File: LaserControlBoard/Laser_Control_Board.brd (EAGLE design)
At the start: 50.8 x 50.8 mm, 36 parts, among them J1 Servo Header, J2 FTDI Header, J5 FEMALE 2x3, J6 455-1750-1-ND, U1 ATMEGA328P_TQFP, Y1 16MHz

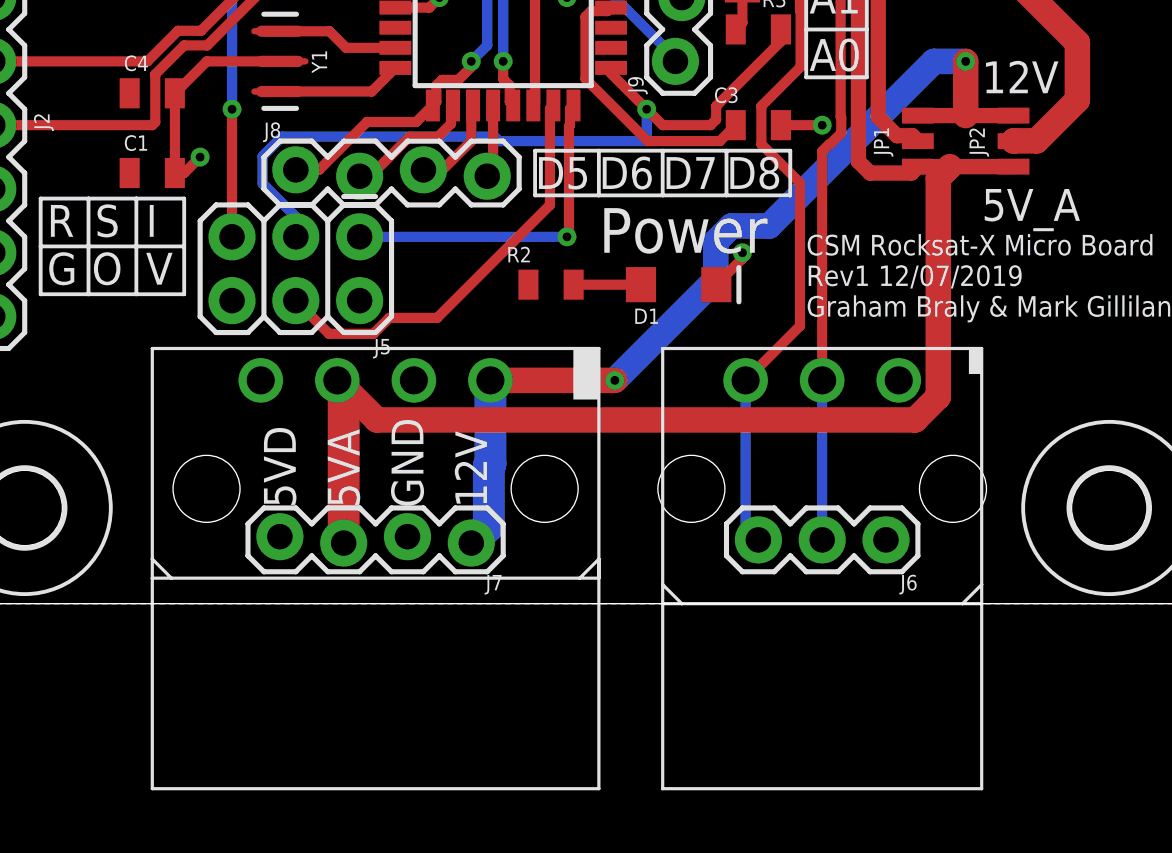
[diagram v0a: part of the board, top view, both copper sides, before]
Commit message: Improved Molex connector footprints.
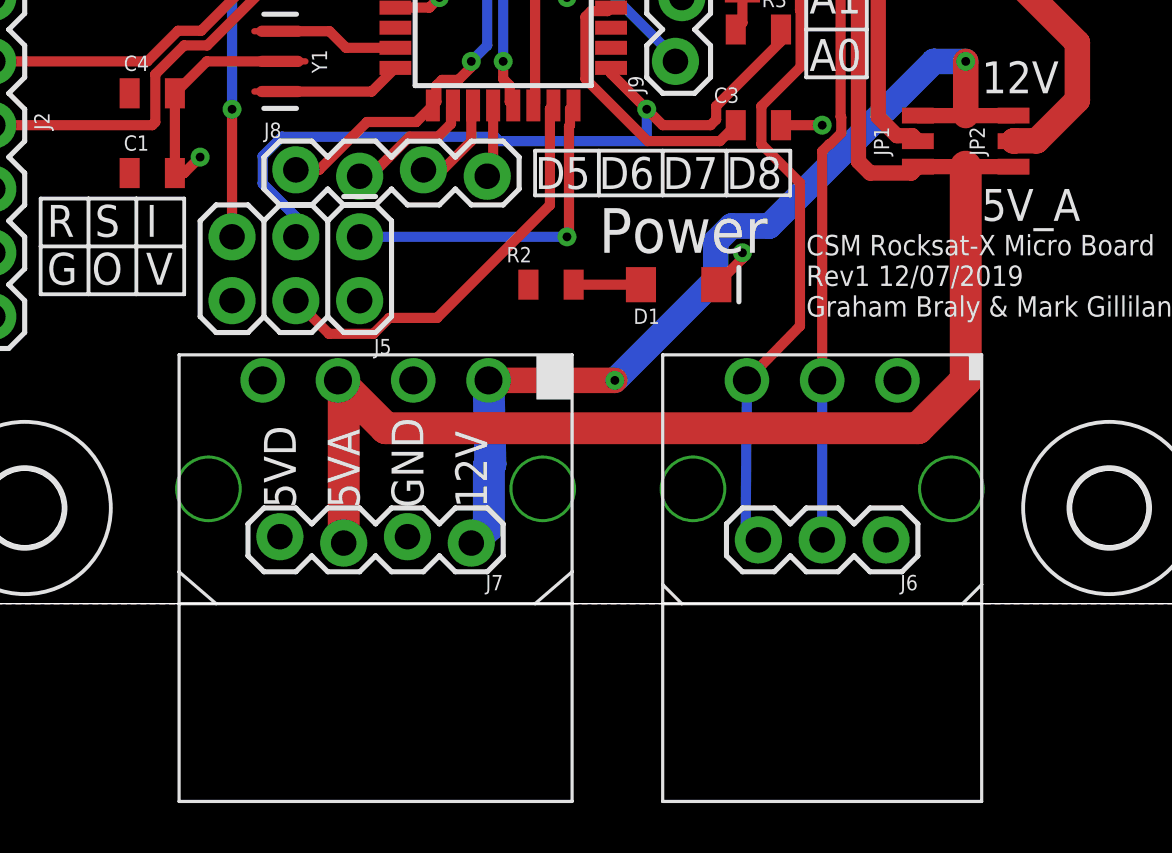
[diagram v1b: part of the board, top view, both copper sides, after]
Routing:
- net 5V_ACT: track 89.7 -> 90.5 mm
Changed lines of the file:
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@@
 <attribute name="VALUE" x="8.89" y="46.228" size="0.6096" layer="27" font="vector" ratio="20"/>
 </element>
-<element name="H1" library="holes" library_urn="urn:adsk.eagle:library:237" package="3,0" package3d_urn="urn:adsk.eagle:package:14277/1" value="MOUNT-HOLE3.0" x="3.81" y="3.81" smashed="yes"/>
-<element name="H2" library="holes" library_urn="urn:adsk.eagle:library:237" package="3,0" package3d_urn="urn:adsk.eagle:package:14277/1" value="MOUNT-HOLE3.0" x="46.99" y="3.81" smashed="yes"/>
-<element name="H3" library="holes" library_urn="urn:adsk.eagle:library:237" package="3,0" package3d_urn="urn:adsk.eagle:package:14277/1" value="MOUNT-HOLE3.0" x="3.81" y="46.99" smashed="yes"/>
-<element name="H4" library="holes" library_urn="urn:adsk.eagle:library:237" package="3,0" package3d_urn="urn:adsk.eagle:package:14277/1" value="MOUNT-HOLE3.0" x="46.99" y="46.99" smashed="yes"/>
+<element name="H1" library="holes" library_urn="urn:adsk.eagle:library:237" package="3,0" package3d_urn="urn:adsk.eagle:package:14277/1" value="MOUNT-HOLE3.0" x="3.81" y="3.81" smashed="yes">
+<attribute name="POPULARITY" value="3" x="3.81" y="3.81" size="1.778" layer="27" display="off"/>
+</element>
+<element name="H2" library="holes" library_urn="urn:adsk.eagle:library:237" package="3,0" package3d_urn="urn:adsk.eagle:package:14277/1" value="MOUNT-HOLE3.0" x="46.99" y="3.81" smashed="yes">
+<attribute name="POPULARITY" value="3" x="46.99" y="3.81" size="1.778" layer="27" display="off"/>
+</element>
+<element name="H3" library="holes" library_urn="urn:adsk.eagle:library:237" package="3,0" package3d_urn="urn:adsk.eagle:package:14277/1" value="MOUNT-HOLE3.0" x="3.81" y="46.99" smashed="yes">
+<attribute name="POPULARITY" value="3" x="3.81" y="46.99" size="1.778" layer="27" display="off"/>
+</element>
+<element name="H4" library="holes" library_urn="urn:adsk.eagle:library:237" package="3,0" package3d_urn="urn:adsk.eagle:package:14277/1" value="MOUNT-HOLE3.0" x="46.99" y="46.99" smashed="yes">
+<attribute name="POPULARITY" value="3" x="46.99" y="46.99" size="1.778" layer="27" display="off"/>
+</element>
 <element name="S1" library="SparkFun-Switches" package="TACTILE_SWITCH_SMD_5.2MM" value="RESET" x="25.4" y="38.1" smashed="yes" rot="R90">
 <attribute name="NAME" x="22.733" y="38.1" size="0.6096" layer="25" font="vector" ratio="20" rot="R90" align="bottom-center"/>
@@
 <element name="D2" library="diode" library_urn="urn:adsk.eagle:library:210" package="SMA" package3d_urn="urn:adsk.eagle:package:43460/3" value="S1M" x="39.37" y="27.94" smashed="yes" rot="R270">
 <attribute name="NAME" x="41.37" y="30.69" size="1.27" layer="25" ratio="10" rot="R270"/>
+<attribute name="POPULARITY" value="0" x="39.37" y="27.94" size="1.778" layer="27" rot="R270" display="off"/>
 <attribute name="VALUE" x="41.585" y="28.15" size="1.27" layer="27" ratio="10" rot="R270"/>
 </element>
@@
 <element name="D4" library="diode" library_urn="urn:adsk.eagle:library:210" package="SMA" package3d_urn="urn:adsk.eagle:package:43460/3" value="S1M" x="45.085" y="27.94" smashed="yes" rot="R270">
 <attribute name="NAME" x="47.085" y="30.69" size="1.27" layer="25" ratio="10" rot="R270"/>
+<attribute name="POPULARITY" value="0" x="45.085" y="27.94" size="1.778" layer="27" rot="R270" display="off"/>
 <attribute name="VALUE" x="47.3" y="28.15" size="1.27" layer="27" ratio="10" rot="R270"/>
 </element>
@@
 <wire x1="39.37" y1="19.431" x2="41.275" y2="19.431" width="0.6096" layer="1"/>
 <wire x1="41.275" y1="19.431" x2="43.18" y2="19.431" width="0.6096" layer="1"/>
-<wire x1="22.352" y1="8.89" x2="27.305" y2="8.89" width="1.016" layer="1"/>
+<wire x1="22.2758" y1="8.89" x2="27.305" y2="8.89" width="1.016" layer="1"/>
 <via x="27.305" y="8.89" extent="1-16" drill="0.35"/>
 <wire x1="40.005" y1="21.59" x2="41.275" y2="21.59" width="1.016" layer="16"/>
@@
 <wire x1="41.275" y1="21.59" x2="41.275" y2="19.431" width="1.016" layer="1"/>
 <contactref element="J7" pad="1"/>
-<wire x1="22.352" y1="8.89" x2="22.352" y2="5.55609375" width="1.27" layer="16"/>
+<wire x1="22.2758" y1="8.89" x2="22.352" y2="5.55609375" width="1.27" layer="16"/>
 <wire x1="22.352" y1="5.55609375" x2="22.2885" y2="5.49259375" width="1.27" layer="16"/>
 <wire x1="22.2885" y1="3.1115" x2="21.59" y2="2.413" width="1.27" layer="16"/>
@@
 <contactref element="JP1" pad="1"/>
 <contactref element="JP2" pad="1"/>
-<wire x1="39.37" y1="17.399" x2="40.64" y2="17.399" width="0.6096" layer="1"/>
-<wire x1="40.64" y1="17.399" x2="43.18" y2="17.399" width="0.6096" layer="1"/>
+<wire x1="39.37" y1="17.399" x2="41.275" y2="17.399" width="0.6096" layer="1"/>
+<wire x1="41.275" y1="17.399" x2="43.18" y2="17.399" width="0.6096" layer="1"/>
 <wire x1="37.005" y1="17.605" x2="37.465" y2="17.145" width="0.6096" layer="1"/>
 <wire x1="37.005" y1="17.605" x2="37.005" y2="27.02105625" width="0.6096" layer="1"/>
 <wire x1="37.465" y1="17.145" x2="39.116" y2="17.145" width="0.6096" layer="1"/>
 <wire x1="39.116" y1="17.145" x2="39.37" y2="17.399" width="0.6096" layer="1"/>
-<wire x1="39.26030625" y1="7.3152" x2="40.1828" y2="8.23769375" width="1.016" layer="1"/>
-<wire x1="40.1828" y1="16.9418" x2="40.64" y2="17.399" width="1.016" layer="1"/>
-<wire x1="40.1828" y1="8.23769375" x2="40.1828" y2="16.9418" width="1.016" layer="1"/>
 <wire x1="28.575" y1="35.45105625" x2="28.575" y2="42.545" width="0.6096" layer="1"/>
 <wire x1="28.575" y1="42.545" x2="26.67" y2="44.45" width="0.6096" layer="1"/>
 <wire x1="26.67" y1="44.45" x2="20.955" y2="44.45" width="0.6096" layer="1"/>
 <wire x1="37.005" y1="27.02105625" x2="28.575" y2="35.45105625" width="0.6096" layer="1"/>
-<wire x1="16.256" y1="8.89" x2="17.8308" y2="7.3152" width="1.016" layer="1"/>
-<wire x1="17.8308" y1="7.3152" x2="39.26030625" y2="7.3152" width="1.016" layer="1"/>
 <contactref element="J7" pad="3"/>
-<wire x1="16.256" y1="8.89" x2="16.51" y2="8.636" width="1.27" layer="1"/>
+<wire x1="16.2814" y1="8.89" x2="16.51" y2="8.636" width="1.27" layer="1"/>
 <wire x1="16.51" y1="8.636" x2="16.51" y2="2.413" width="1.27" layer="1"/>
+<wire x1="16.2814" y1="8.89" x2="18.1864" y2="6.985" width="1.27" layer="1"/>
+<wire x1="39.37" y1="6.985" x2="41.275" y2="8.89" width="1.27" layer="1"/>
+<wire x1="41.275" y1="8.89" x2="41.275" y2="17.399" width="1.27" layer="1"/>
+<wire x1="18.1864" y1="6.985" x2="39.37" y2="6.985" width="1.27" layer="1"/>
 </signal>
 <signal name="SDA">
@@
 <wire x1="24.06" y1="28.4226" x2="24.1996" y2="28.5622" width="0.4064" layer="1"/>
 <wire x1="24.1996" y1="28.5622" x2="24.1996" y2="29.2154125" width="0.4064" layer="1"/>
-<wire x1="34.6756" y1="11.0536" x2="32.512" y2="8.89" width="0.4064" layer="1"/>
+<wire x1="34.6756" y1="11.0536" x2="32.5628" y2="8.89" width="0.4064" layer="1"/>
 <wire x1="34.6756" y1="27.5544" x2="34.6756" y2="23.6432125" width="0.4064" layer="1"/>
 <wire x1="34.6756" y1="23.6432125" x2="34.701" y2="23.6178125" width="0.4064" layer="1"/>
@@
 <wire x1="25.5149875" y1="30.5308" x2="31.6992" y2="30.5308" width="0.4064" layer="1"/>
 <wire x1="31.6992" y1="30.5308" x2="34.6756" y2="27.5544" width="0.4064" layer="1"/>
-<wire x1="32.512" y1="8.89" x2="32.512" y2="3.048" width="0.4064" layer="16"/>
+<wire x1="32.5628" y1="8.89" x2="32.512" y2="3.048" width="0.4064" layer="16"/>
 <wire x1="32.512" y1="3.048" x2="33.02" y2="2.54" width="0.4064" layer="16"/>
 </signal>

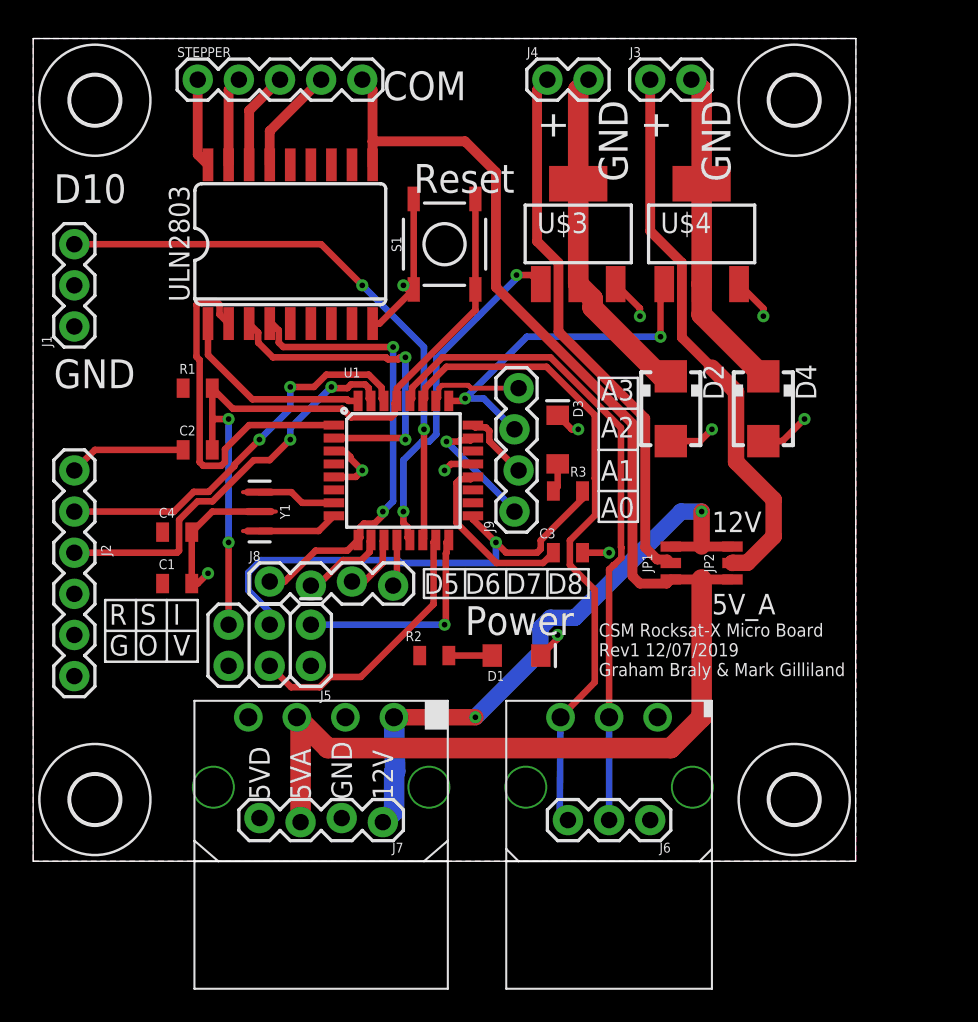
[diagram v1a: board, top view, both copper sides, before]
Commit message: Lots of Labels added, GND connections added, component labels embiggened, traces rerouted.
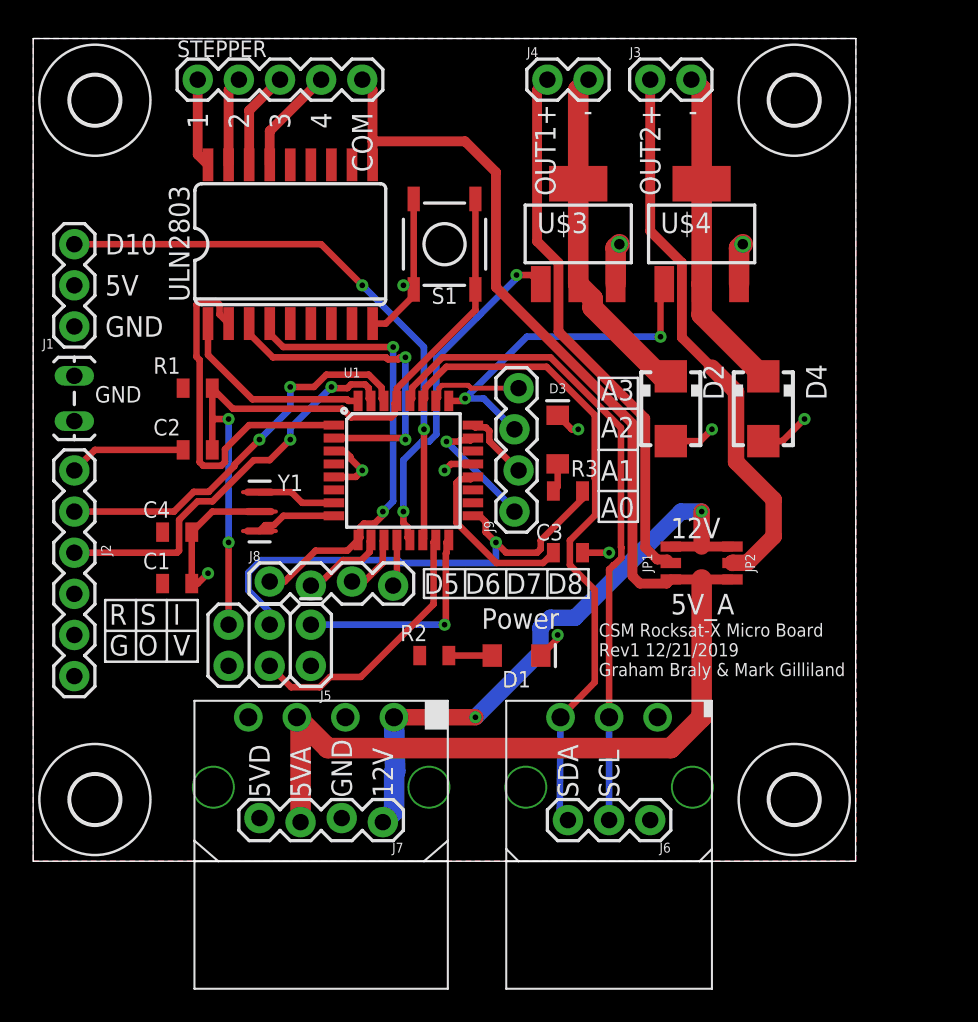
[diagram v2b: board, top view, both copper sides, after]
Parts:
- added GND: (no value), SparkFun-Connectors:1X02_LOCK_LONGPADS
- D1, D3: value GREEN -> (none)
- J1: value Servo Header -> Servo
- J2: value FTDI Header -> FTDI
- J6: value 455-1750-1-ND -> (none)
- U$3, U$4: value BUK9880-55A -> (none)
- U1: value ATMEGA328P_TQFP -> ATMEGA328P
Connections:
- net GND: now also GND.1, GND.2
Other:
- board text added: "-"
- board text added: "1"
- board text added: "2"
- board text added: "3"
- board text added: "4"
- board text added: "5V"
- board text added: "CSM Rocksat-X Micro Board Rev1 12/21/2019 Graham Braly & Mark Gilliland"
- board text added: "OUT1+"
- board text added: "OUT2+"
- board text added: "SCL"
- board text added: "SDA"
- board text removed: "+"
- board text removed: "CSM Rocksat-X Micro Board Rev1 12/07/2019 Graham Braly & Mark Gilliland"
- board text removed: "Reset"

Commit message: Changed silkscreen for clarity
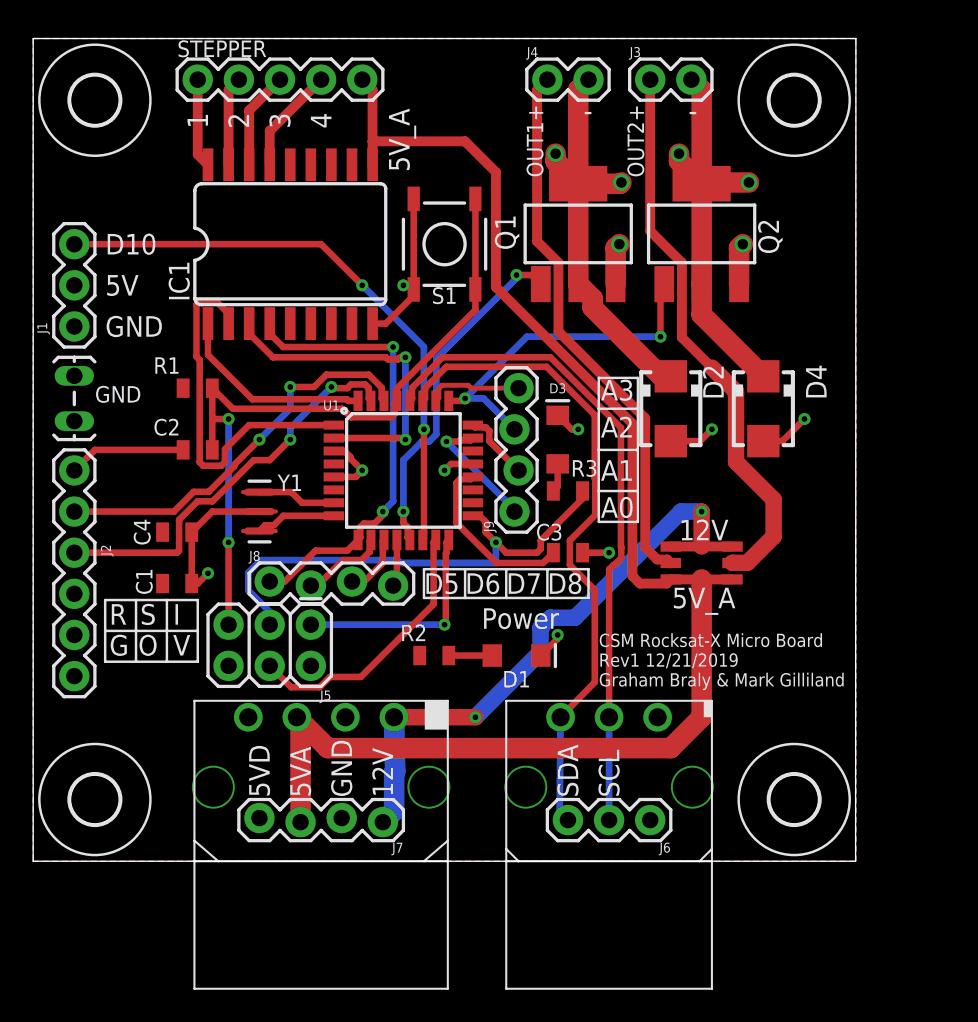
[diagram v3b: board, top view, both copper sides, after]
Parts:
- IC1: value (none) -> ULN2803
- renumbered U$3 to Q1, U$4 to Q2, ULN2803 to IC1
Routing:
- net MOSFET_SWITCHED_2: track 20.2 -> 25.5 mm, vias 0 -> 2
- net MOSFET_SWITCHED_1: track 21.3 -> 26.4 mm, vias 0 -> 2
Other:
- board text added: "OUT1"
- board text added: "OUT2"
